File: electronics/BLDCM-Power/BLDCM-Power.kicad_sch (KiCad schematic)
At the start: 37 parts, among them J1 501920-3001, J2 53048-0310, J3 53261-0471, J4 53261-0471, J5 FTSH-107-01-L-DV-K, J6 12402012E212A, U1 INA239-Q1, U2 LDL212PV33R, U3 TMC6300-LA, U4 INA239-Q1, U5 TCAN1462, U6 INA239-Q1

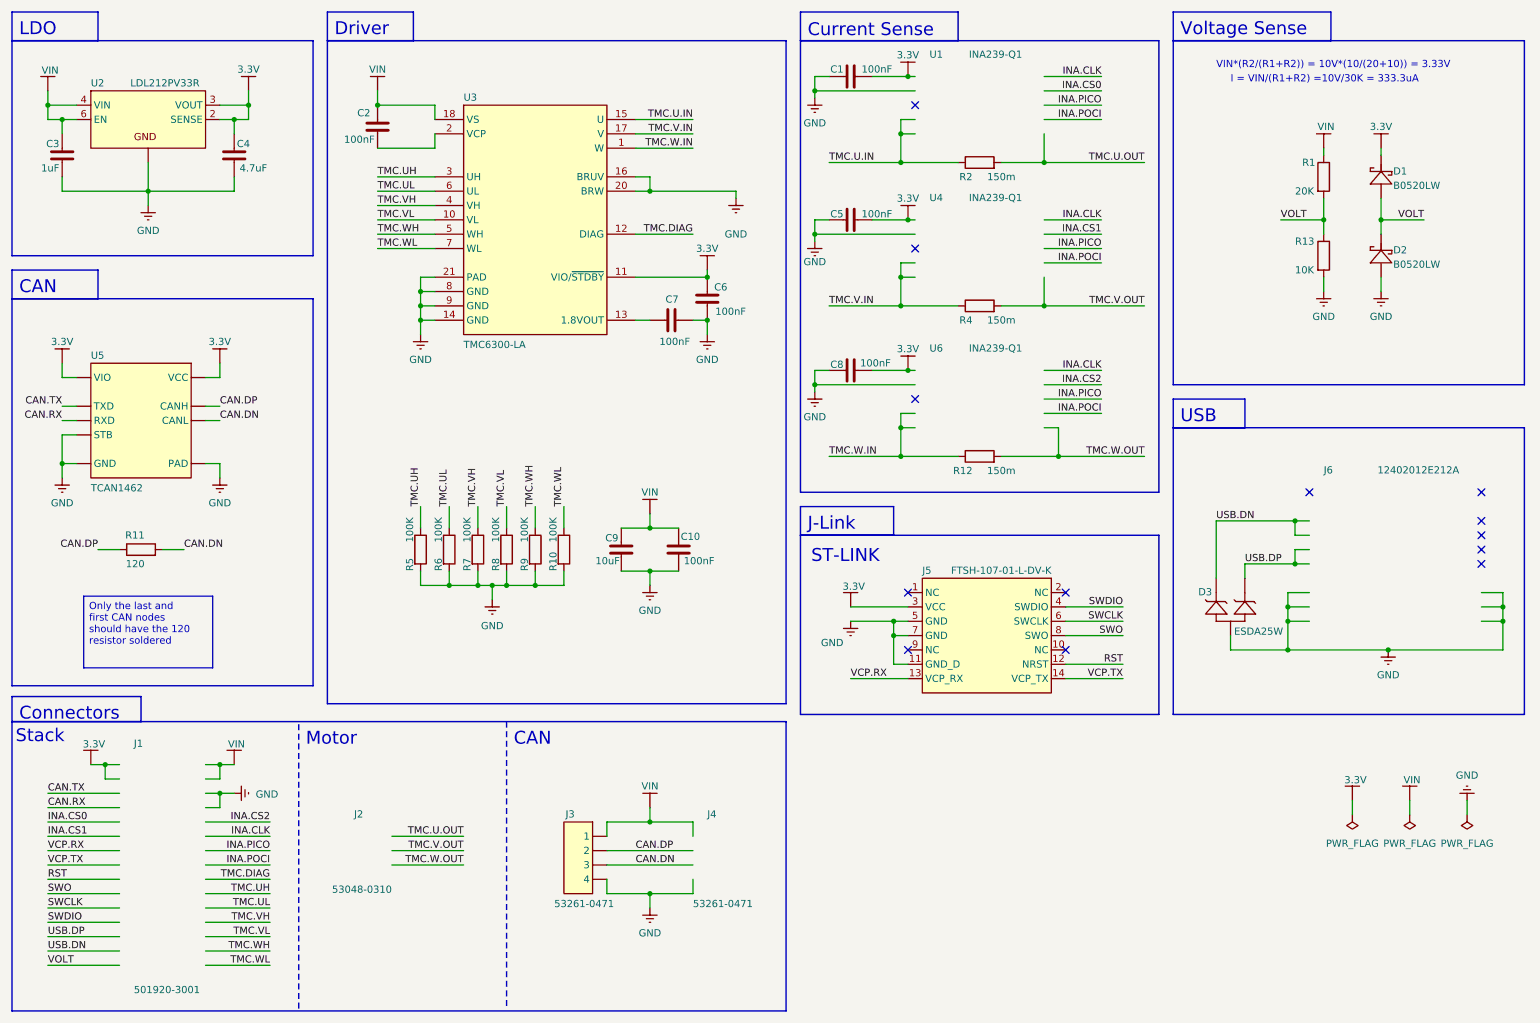
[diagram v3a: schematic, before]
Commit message: Feat(pcb): Add power management sheet
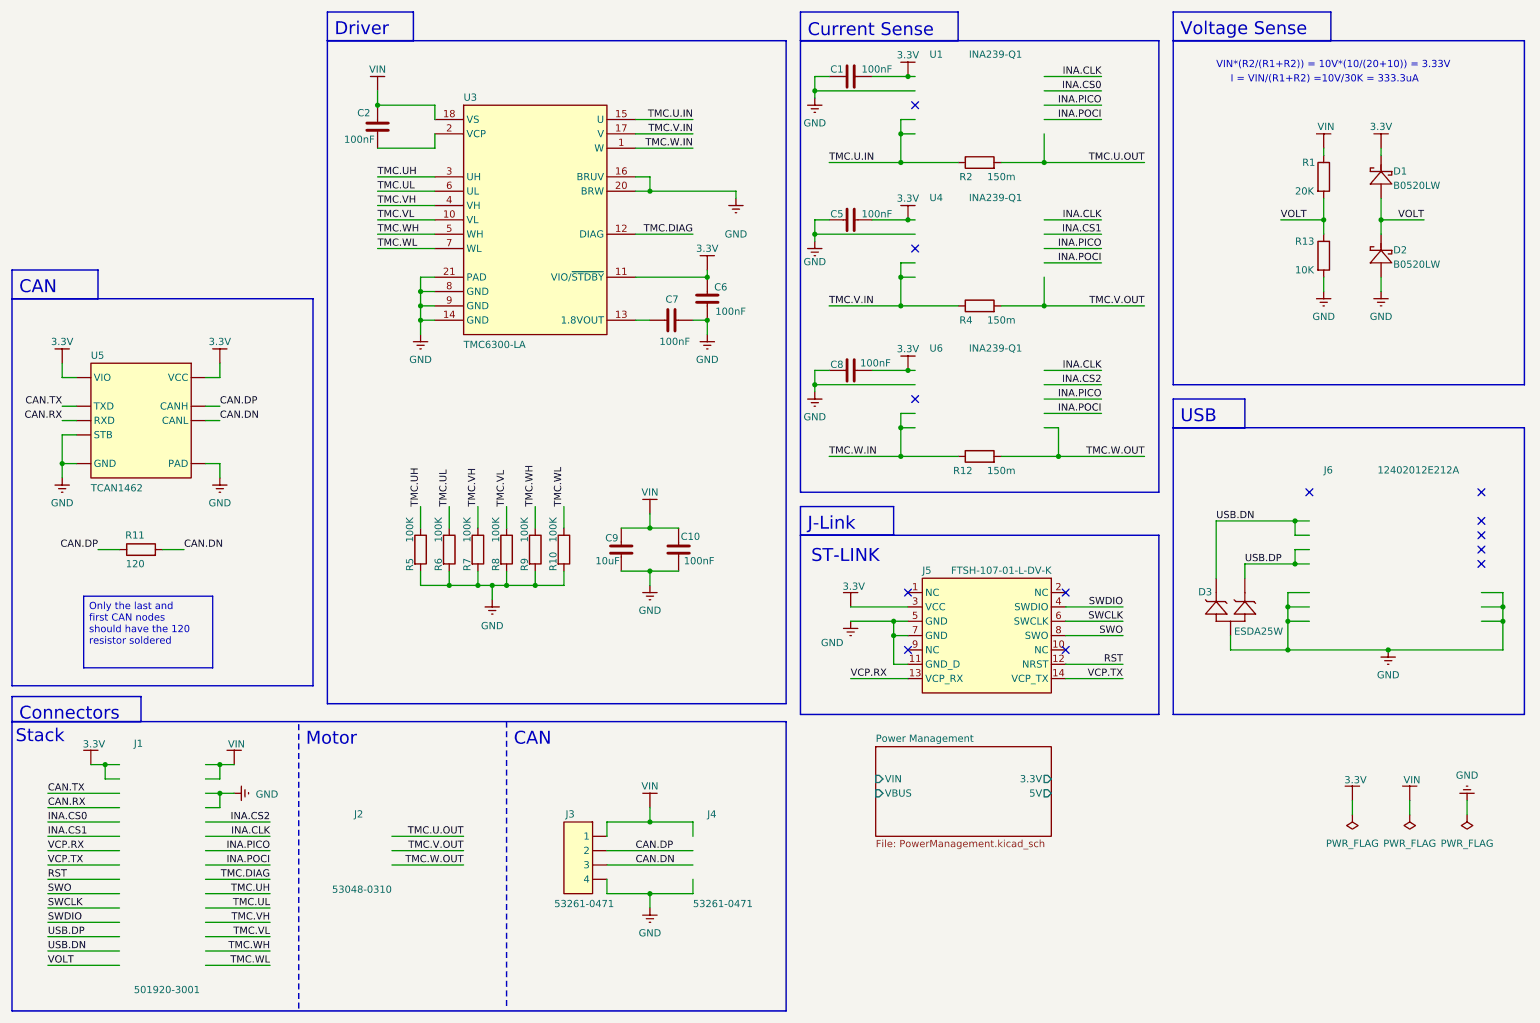
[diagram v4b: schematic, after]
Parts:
- removed C3: 1uF, BrenoCQ:C_0402, symbol BrenoCQ:C
- removed C4: 4.7uF, BrenoCQ:C_0402, symbol BrenoCQ:C
- removed U2: LDL212PV33R, BrenoCQ:DFN-6-2x2, symbol BrenoCQ:LDL212PV33R
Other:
- added sheet Power Management (PowerManagement.kicad_sch)
- note removed: "LDO"

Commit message: Fix(pcb): Add missing USB CC1 pull-down
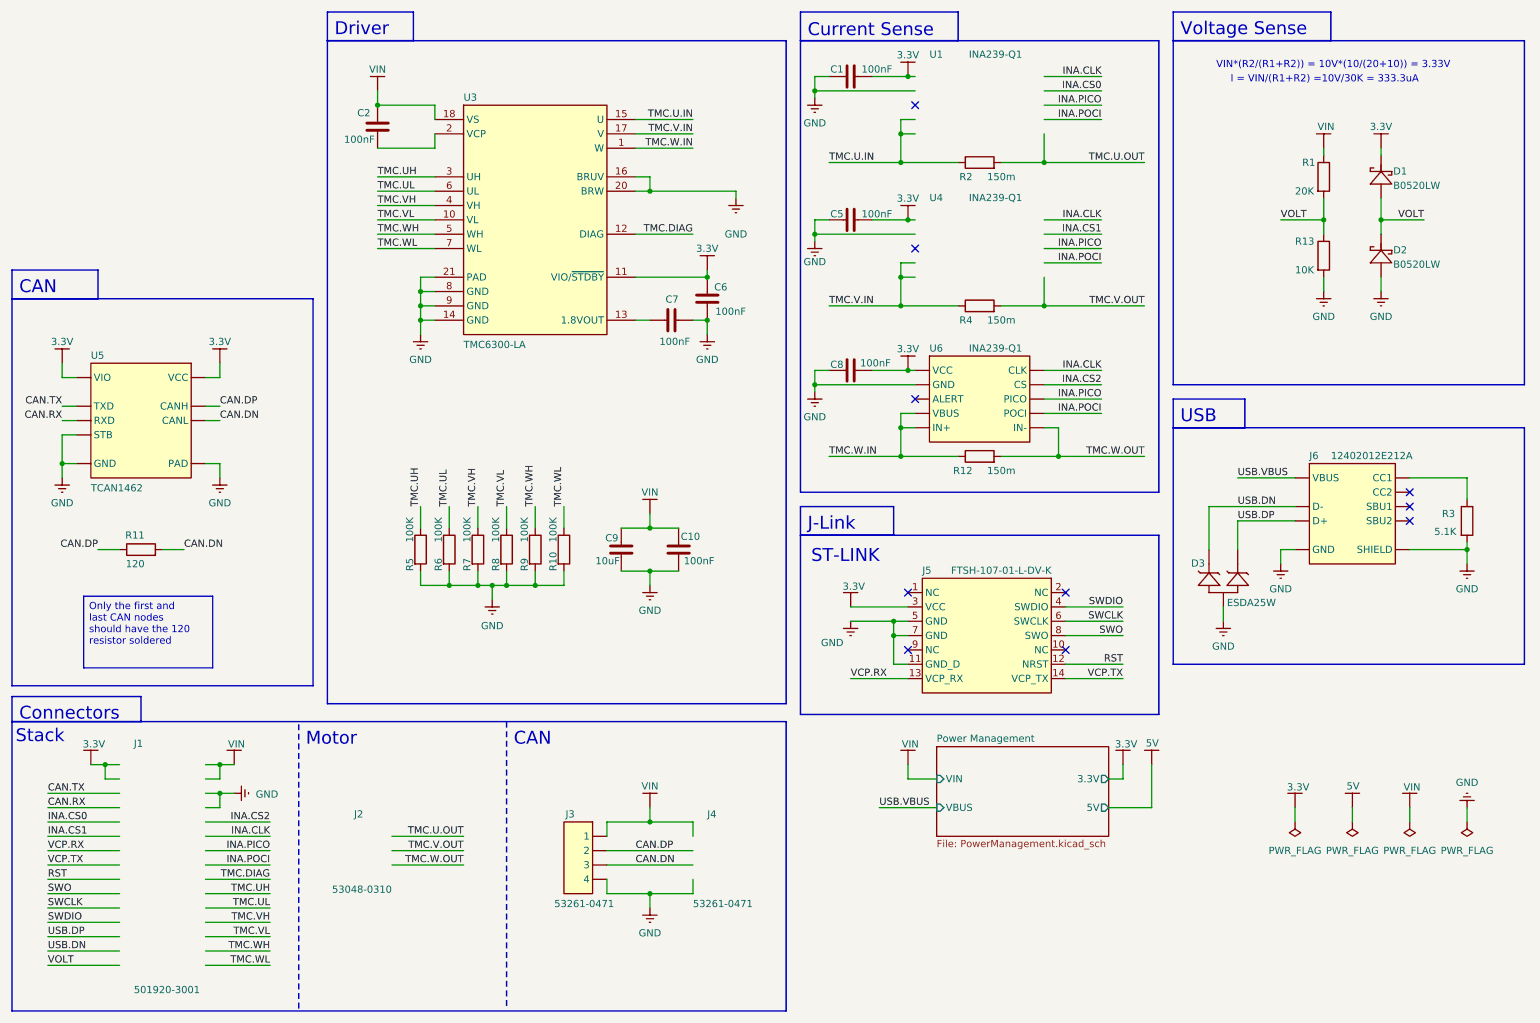
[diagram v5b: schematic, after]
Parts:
- added R3: 5.1K, BrenoCQ:R_0402, symbol Device:R
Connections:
- net 3.3V: now also U6.6 (VCC)
- net GND: now also J6.A1_B12 (GND), J6.B1_A12 (GND), J6.SH1 (SHIELD), J6.SH2 (SHIELD), J6.SH3 (SHIELD), J6.SH4 (SHIELD), U6.7 (GND), R3.2
- net INA.CLK: now also U6.5 (CLK)
- net INA.CS2: now also U6.1 (CS)
- net INA.PICO: now also U6.2 (PICO)
- net INA.POCI: now also U6.4 (POCI)
- net TMC.W.IN: now also U6.10 (IN+), U6.8 (VBUS)
- net TMC.W.OUT: now also U6.9 (IN-)
- net USB.DN: now also J6.A7 (D-), J6.B7 (D-2)
- net USB.DP: now also J6.A6 (D+), J6.B6 (D+2)
- new net: J6.A5 (CC1), R3.1
- new net VBUS: J6.A4_B9 (VBUS), J6.B4_A9 (VBUS)
- no-connect marks 13 -> 10
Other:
- moved on the sheet: D3

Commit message: Feat(schematic): Automatic power source selection
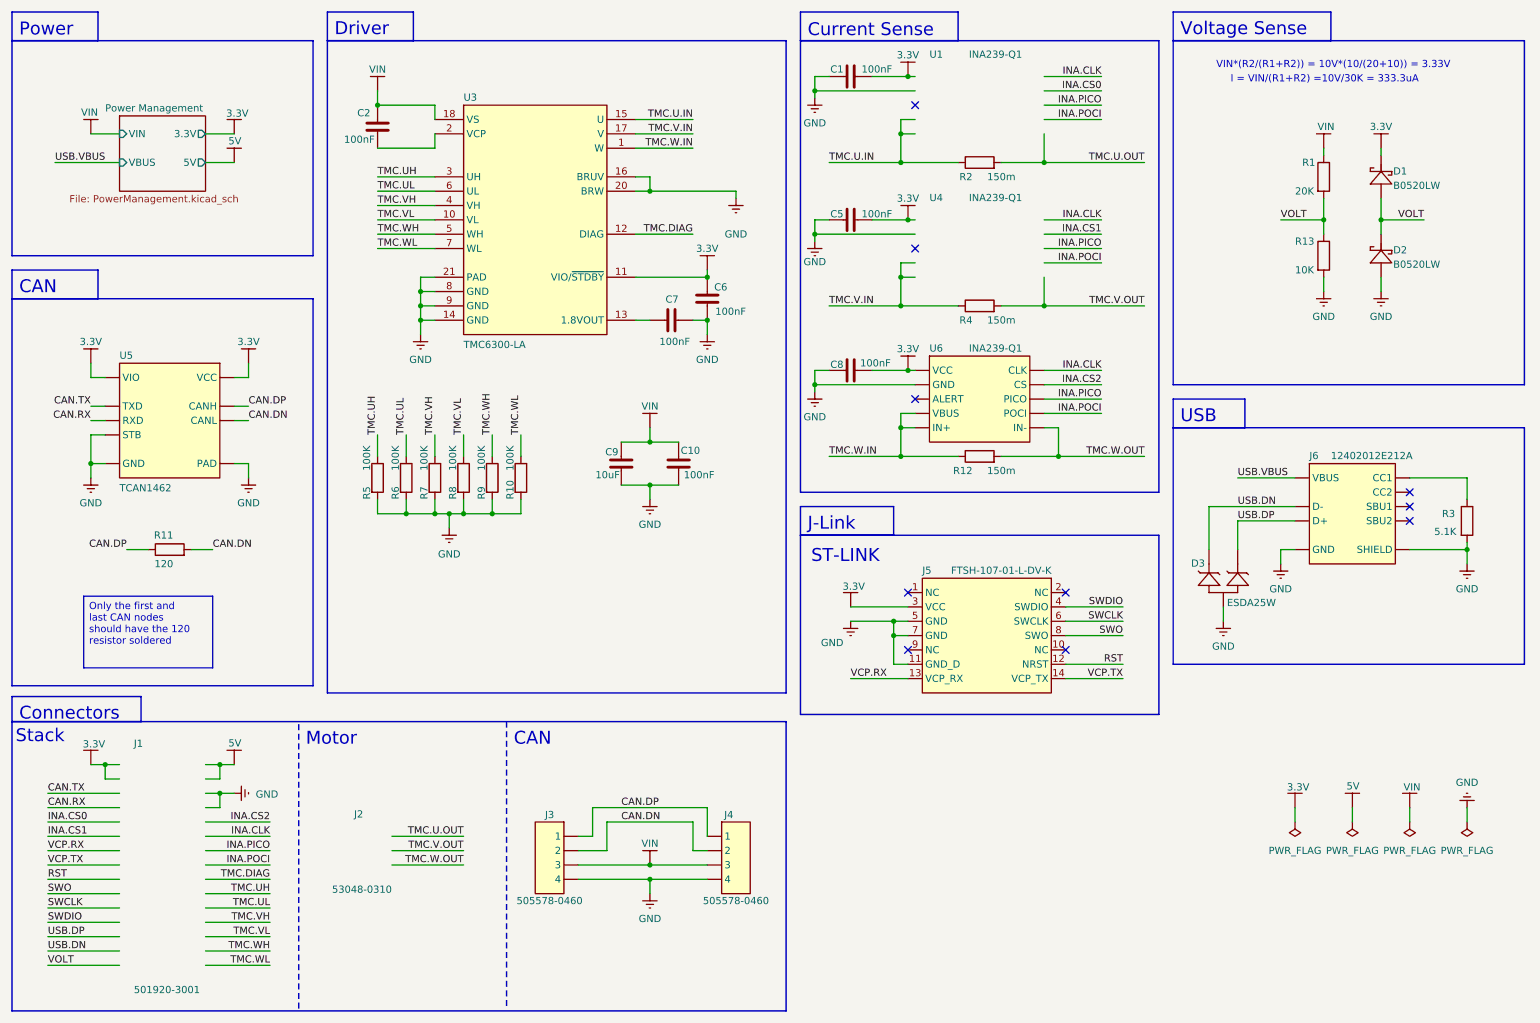
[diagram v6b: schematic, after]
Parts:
- removed J3, J4: 53261-0471, BrenoCQ:53261-0471, symbol BrenoCQ:Molex_125MM-4P-H-SMD
- added J3, J4: 505578-0460, BrenoCQ:505578-0460, symbol BrenoCQ:Molex_MicroLock_2MM-4P-H-SMD
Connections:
- net CAN.DN: now also J3.2, J4.2
- net CAN.DP: now also J3.1, J4.1
- net GND: now also J3.4, J4.4
- net VIN: now also J3.3, J4.3
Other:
- note added: "Power"
- moved on the sheet: C10, C9, R10, R11, R5, R6, R7, R8, R9, U5

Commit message: Feat(schematic): Update volt sense to use BAT54S
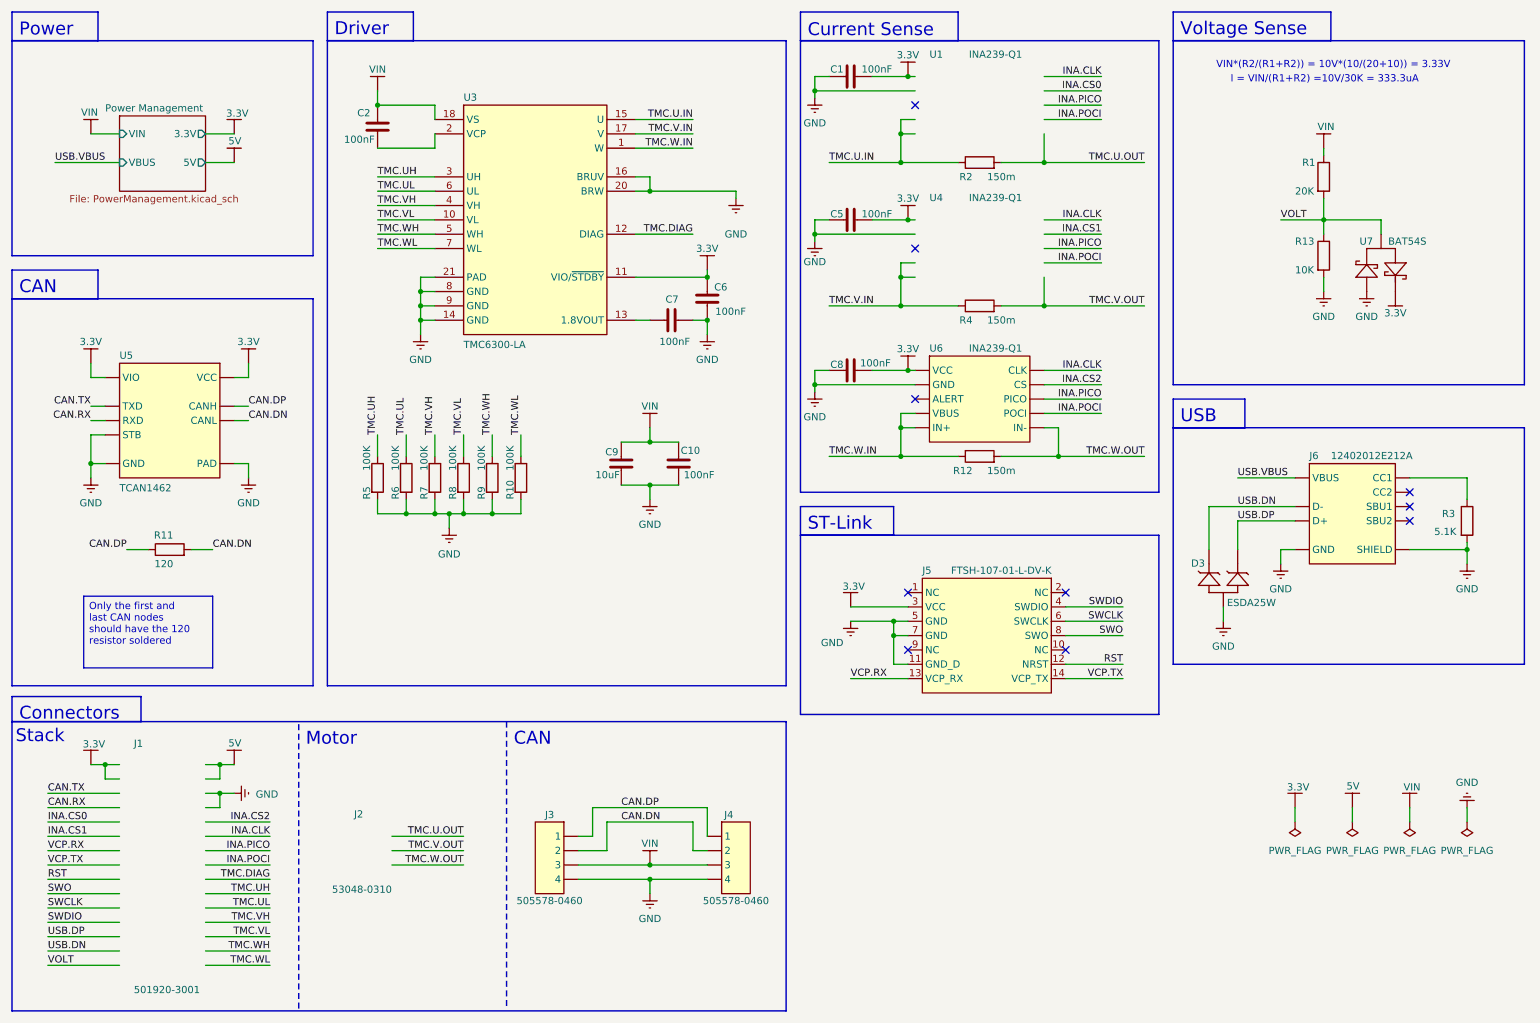
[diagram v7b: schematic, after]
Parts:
- removed D1, D2: B0520LW, BrenoCQ:SOD-123, symbol BrenoCQ:D_Schottky_B0520LW
- added U7: BAT54S, BrenoCQ:SOT-23, symbol BrenoCQ:BAT54S
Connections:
- net 3.3V: now also U7.2
- net GND: now also U7.1
- net VOLT: now also U7.3
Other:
- note added: "ST-Link"
- note removed: "J-Link"
- note removed: "ST-LINK"

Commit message: Feat(schematic): Replace current sense resistors
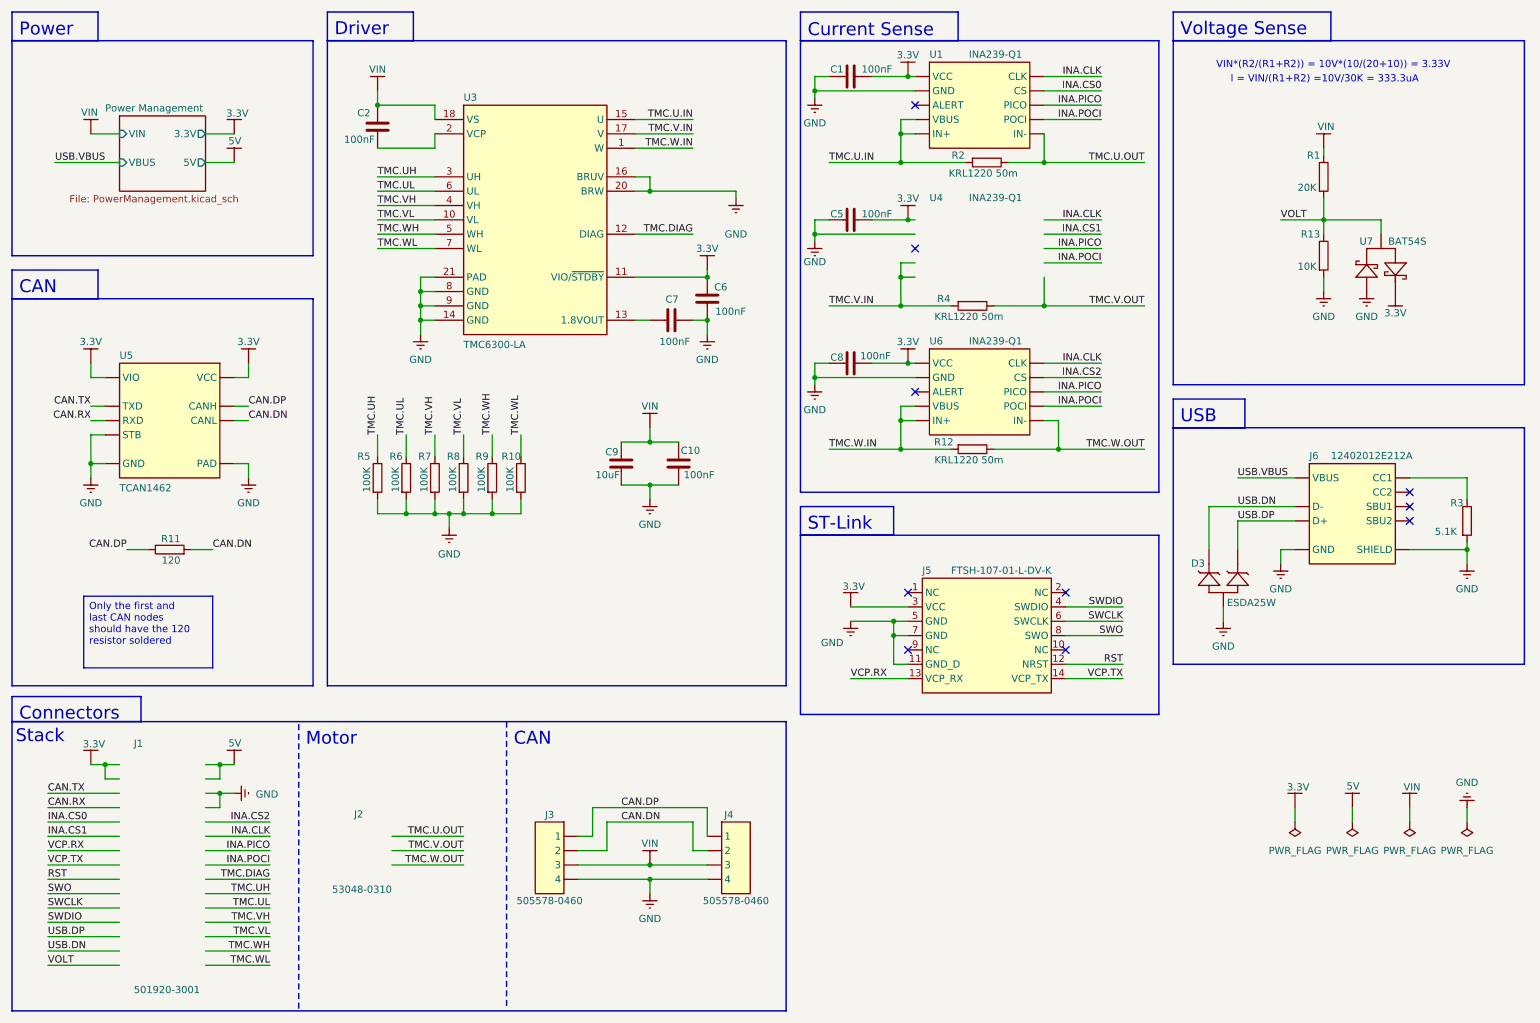
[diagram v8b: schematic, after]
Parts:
- removed R12, R2, R4: 150m, BrenoCQ:R_1210, symbol Device:R
- added R12, R2, R4: KRL1220 50m, BrenoCQ:KRL1220, symbol BrenoCQ:R_KRL1220
- R1, R10, R11, R13, R3, R5, R6, R7, R8, R9: symbol Device:R -> BrenoCQ:R
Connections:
- net 3.3V: now also U1.6 (VCC)
- net CAN.DN: now also R11.1; no longer R11.2
- net CAN.DP: now also R11.2; no longer R11.1
- net GND: now also R10.1, R13.1, R3.1, R5.1, R6.1, R7.1, R8.1, R9.1, U1.7 (GND); no longer R10.2, R13.2, R3.2, R5.2, R6.2, R7.2, R8.2, R9.2
- net INA.CLK: now also U1.5 (CLK)
- net INA.CS0: now also U1.1 (CS)
- net INA.PICO: now also U1.2 (PICO)
- net INA.POCI: now also U1.4 (POCI)
- net TMC.U.IN: now also U1.10 (IN+), U1.8 (VBUS), R2.1
- net TMC.U.OUT: now also U1.9 (IN-), R2.2
- net TMC.UH: now also R5.2; no longer R5.1
- net TMC.UL: now also R6.2; no longer R6.1
- net TMC.V.IN: now also R4.1
- net TMC.V.OUT: now also R4.2
- net TMC.VH: now also R7.2; no longer R7.1
- net TMC.VL: now also R8.2; no longer R8.1
- net TMC.W.IN: now also R12.1
- net TMC.W.OUT: now also R12.2
- net TMC.WH: now also R9.2; no longer R9.1
- net TMC.WL: now also R10.2; no longer R10.1
- net VIN: now also R1.2; no longer R1.1
- net VOLT: now also R1.1, R13.2; no longer R1.2, R13.1
- net at J6.A5 (CC1): now also R3.2; no longer R3.1
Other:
- moved on the sheet: C8, R1, R10, R11, R13, R3, R5, R6, R7, R8, R9, U6
